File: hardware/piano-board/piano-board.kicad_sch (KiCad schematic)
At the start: 32 parts, among them J1 AVR-ISP-6, Q1 Q_NMOS_GSD, Q2 Q_PMOS_GSD, SW1 SW_SPDT, SW2 OCT_INC, SW3 OCT_DWN, SW4 WAVE_CHANGE, U1 ATmega328PB-A

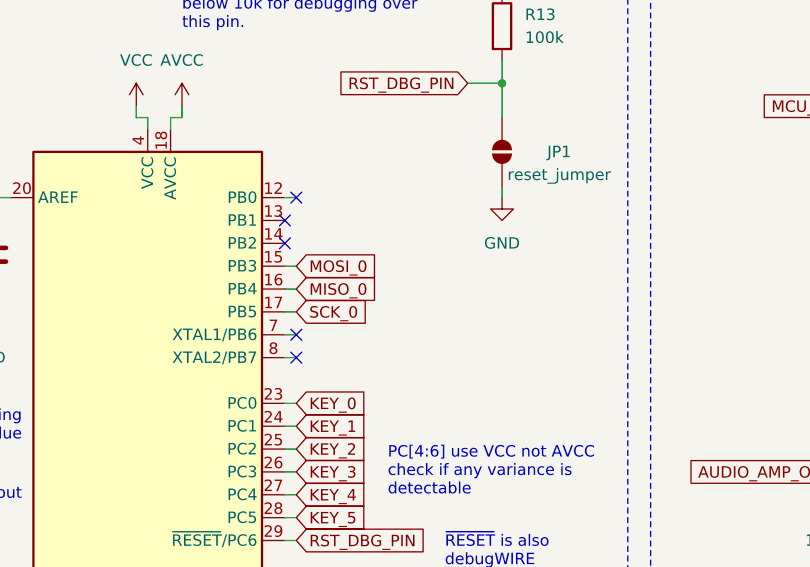
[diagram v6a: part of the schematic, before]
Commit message: Add status LED
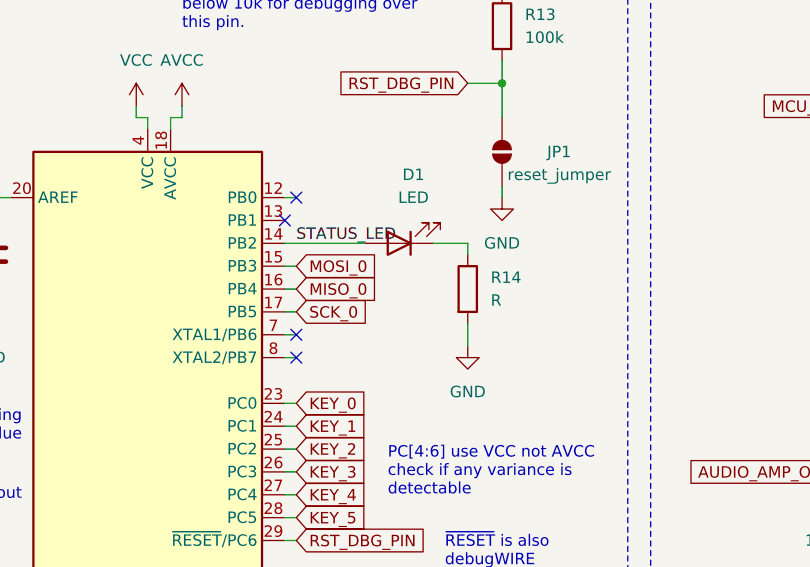
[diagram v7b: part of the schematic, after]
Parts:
- added D1: LED, LED_SMD:LED_0603_1608Metric_Pad1.05x0.95mm_HandSolder, symbol Device:LED
- added R14: R, Resistor_SMD:R_0603_1608Metric_Pad0.98x0.95mm_HandSolder, symbol Device:R
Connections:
- net GND: now also R14.2
- net STATUS_LED: now reaches U1.14 (PB2)
- net STATUS_LED: now also D1.2 (A)
- new net: D1.1 (K), R14.1
- no-connect marks 8 -> 7

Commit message: Polish for manufacturing
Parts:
- added R15: 0, Resistor_SMD:R_0603_1608Metric_Pad0.98x0.95mm_HandSolder, symbol Device:R
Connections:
- net AUDIO_AMP_OUT: now also Q1.3 (D), Q2.3 (D); no longer Q1.2 (S), Q2.2 (S)
- net AUDIO_FLTR_OUT: now also R15.1; no longer LS1.1
- net AVCC: now also Q2.2 (S); no longer Q2.3 (D)
- net GND: now also Q1.2 (S); no longer Q1.3 (D)
- new net: LS1.1, R15.2
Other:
- note added: "Class D audio amplifier"
- note added: "Resistor for tuning volume"
- note removed: "The audio output implements a class D amplifier"
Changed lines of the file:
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@@
 	(wire
 		(pts
+			(xy 233.68 113.03) (xy 234.95 113.03)
+		)
+		(stroke
+			(width 0)
+			(type default)
+		)
+	)
+	(wire
+		(pts
 			(xy 172.72 85.09) (xy 173.99 85.09)
 		)
@@
 		)
 	)
-	(text "The audio output implements \na class D amplifier"
+	(text "Class D audio amplifier"
 		(exclude_from_sim no)
 		(at 246.38 69.85 0)
@@
 		)
 	)
+	(text "Resistor for tuning volume"
+		(exclude_from_sim no)
+		(at 231.14 118.11 0)
+		(effects
+			(font
+				(size 1.27 1.27)
+			)
+		)
+	)
 	(text "PC[4:6] use VCC not AVCC\ncheck if any variance is\ndetectable"
 		(exclude_from_sim no)
@@
 	(global_label "AUDIO_FLTR_OUT"
 		(shape input)
-		(at 242.57 113.03 180)
+		(at 233.68 113.03 180)
 		(fields_autoplaced yes)
 		(effects
@@
 		)
 		(property "Intersheetrefs" "${INTERSHEET_REFS}"
-			(at 224.0423 113.03 0)
+			(at 215.1523 113.03 0)
 			(effects
 				(font
@@
 		(lib_id "Device:Q_PMOS_GSD")
 		(at 248.92 33.02 0)
+		(mirror x)
 		(unit 1)
 		(exclude_from_sim no)
@@
 		(dnp no)
 		(property "Reference" "Q2"
-			(at 255.27 34.2901 0)
+			(at 255.27 31.7499 0)
 			(effects
 				(font
@@
 		)
 		(property "Value" "Q_PMOS_GSD"
-			(at 255.27 31.7501 0)
+			(at 255.27 34.2899 0)
 			(effects
 				(font
@@
 		)
 		(property "Footprint" "Package_TO_SOT_SMD:SOT-23"
-			(at 254 30.48 0)
+			(at 254 35.56 0)
 			(effects
 				(font
@@
 		(lib_id "Device:Q_NMOS_GSD")
 		(at 248.92 49.53 0)
-		(mirror x)
 		(unit 1)
 		(exclude_from_sim no)
@@
 		(on_board yes)
 		(dnp no)
-		(fields_autoplaced yes)
 		(property "Reference" "Q1"
-			(at 255.27 48.2599 0)
+			(at 255.27 50.8001 0)
 			(effects
 				(font
@@
 		)
 		(property "Value" "Q_NMOS_GSD"
-			(at 255.27 50.7999 0)
+			(at 255.27 48.2601 0)
 			(effects
 				(font
@@
 		)
 		(property "Footprint" "Package_TO_SOT_SMD:SOT-23"
-			(at 254 52.07 0)
+			(at 254 46.99 0)
 			(effects
 				(font
@@
 					(unit 1)
 				)
+			)
+		)
+	)
+	(symbol
+		(lib_id "Device:R")
+		(at 238.76 113.03 90)
+		(unit 1)
+		(exclude_from_sim no)
+		(in_bom yes)
+		(on_board yes)
+		(dnp no)
+		(fields_autoplaced yes)
+		(property "Reference" "R15"
+			(at 238.76 106.68 90)
+			(effects
+				(font
+					(size 1.27 1.27)
+				)
+			)
+		)
+		(property "Value" "0"
+			(at 238.76 109.22 90)
+			(effects
+				(font
+					(size 1.27 1.27)
+				)
+			)
+		)
+		(property "Footprint" "Resistor_SMD:R_0603_1608Metric_Pad0.98x0.95mm_HandSolder"
+			(at 238.76 114.808 90)
+			(effects
+				(font
+					(size 1.27 1.27)
+				)
+				(hide yes)
+			)
+		)
+		(property "Datasheet" "~"
+			(at 238.76 113.03 0)
+			(effects
+				(font
+					(size 1.27 1.27)
+				)
+				(hide yes)
+			)
+		)
+		(property "Description" "Resistor"
+			(at 238.76 113.03 0)
+			(effects
+				(font
+					(size 1.27 1.27)
+				)
+				(hide yes)
+			)
+		)
+		(pin "1"
+		)
+		(pin "2"
+		)
+		(instances
+			(project "piano-board"
+				(path "/02862e3b-5808-4b96-99c1-d327c4a2b9d4"
+					(reference "R15")
+					(unit 1)
+				)
